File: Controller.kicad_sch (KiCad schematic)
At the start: 28 parts, among them IC3 STM32H563VGT6, U4 BMI088

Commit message: new update
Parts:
- removed C29, C30: 100nF, C0402C104K4RAC:CAPC1005X55N, symbol C0402C104K4RAC:C0402C104K4RAC
- removed U4: BMI088, Module:PQFN50P450X300X100-16N, symbol BMI088:BMI088
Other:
- moved on the sheet: R18

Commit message: new
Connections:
- net SCK: now reaches IC3.1 (PE2)
- net AR_A4: now reaches IC3.15 (PC0)
- net ETH_MDC: now reaches IC3.16 (PC1)
- net AR_A5: now reaches IC3.17 (PC2)
- net AR_MOSI: now reaches IC3.18 (PC3)
- net 50MHZOUT: now reaches IC3.24 (PA1)
- net ETH_MDIO: now reaches IC3.25 (PA2)
- net AR_SS: now reaches IC3.26 (PA3)
- net AR_A0: now reaches IC3.29 (PA4)
- net ETH_TX_EN: now reaches IC3.30 (PA5)
- net AR_A1: now reaches IC3.31 (PA6)
- net ETH_CRS_DV: now reaches IC3.32 (PA7)
- net ETH_RX_D0: now reaches IC3.33 (PC4)
- net ETH_RX_D1: now reaches IC3.34 (PC5)
- net AR_A2: now reaches IC3.35 (PB0)
- net AR_A3: now reaches IC3.36 (PB1)
- net SDI: now reaches IC3.4 (PE5)
- net ESP_BOOT: now reaches IC3.44 (PE13)
- net ESP_EN: now reaches IC3.45 (PE14)
- net SDO: now reaches IC3.5 (PE6)
- net ETH_TX_D0: now reaches IC3.51 (PB12)
- net AR_SCK: now reaches IC3.52 (PB13)
- net AR_MISO: now reaches IC3.53 (PB14)
- net ETH_TX_D1: now reaches IC3.54 (PB15)
- net AR_TX: now reaches IC3.55 (PD8)
- net AR_RX: now reaches IC3.56 (PD9)
- net AR_D4: now reaches IC3.57 (PD10)
- net AR_D5: now reaches IC3.58 (PD11)
- net AR_D6: now reaches IC3.59 (PD12)
- net AR_D7: now reaches IC3.60 (PD13)
- net AR_D8: now reaches IC3.61 (PD14)
- net AR_D9: now reaches IC3.62 (PD15)
- net AR_D2: now reaches IC3.63 (PC6)
- net AR_D3: now reaches IC3.64 (PC7)
- net ESP_TXD: now reaches IC3.68 (PA9)
- net ESP_RXD: now reaches IC3.69 (PA10)
- net GN_CS: now reaches IC3.77 (PA15)
- net GN_SDO: now reaches IC3.87 (PD6)
- net GN_SCK: now reaches IC3.89 (PB3)
- net GN_SDI: now reaches IC3.90 (PB4)
- net GN_TIMEPULSE: now reaches IC3.91 (PB5)
- net AR_SCL: now reaches IC3.92 (PB6)
- net AR_SDA: now reaches IC3.93 (PB7)
- net TX_READY: now reaches IC3.95 (PB8)
- net GN_EXINT: now reaches IC3.96 (PB9)

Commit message: new table
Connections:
- net CSB_ACCEL: now also IC3.42 (PE11)
- net CSB_GYRO: now also IC3.3 (PE4)
- net INT1_ACCEL: now also IC3.2 (PE3)
- net INT1_GYRO: now also IC3.8 (PC14-OSC32_IN)
- net INT2_ACCEL: now also IC3.7 (PC13)
- net INT2_GYRO: now also IC3.9 (PC15-OSC32_OUT)
- net RESET_GNSS: now also IC3.97 (PE0)
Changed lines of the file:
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@@
-		)
-	)
-	(text_box "CHECK THE PIN MAPPING FOR IMU"
-		(exclude_from_sim no)
-		(at 85.09 36.83 0)
-		(size 33.02 21.59)
-		(stroke
-			(width 0)
-			(type default)
-		)
-		(fill
-			(type color)
-			(color 114 255 146 1)
-		)
-		(effects
-			(font
-				(size 2.54 2.54)
-				(thickness 0.254)
-				(bold yes)
-			)
-			(justify left top)
-		)
-	)
-	(text_box "THE PIN MAPPING FOR GNSS RESET AND AR_A2 HAVE THE SAME PIN IN STM."
-		(exclude_from_sim no)
-		(at 33.02 33.02 0)
-		(size 35.56 26.67)
-		(stroke
-			(width 0)
-			(type default)
-		)
-		(fill
-			(type color)
-			(color 140 255 96 1)
-		)
-		(effects
-			(font
-				(size 2.54 2.54)
-			)
-			(justify left top)
 		)
 	)
@@
 	(global_label "INT2_ACCEL"
 		(shape input)
-		(at 106.68 52.07 0)
-		(fields_autoplaced yes)
-		(effects
-			(font
-				(size 1.27 1.27)
-			)
-			(justify left)
-		)
-		(property "Intersheetrefs" "${INTERSHEET_REFS}"
-			(at 120.5509 52.07 0)
-			(effects
-				(font
-					(size 1.27 1.27)
-				)
-				(justify left)
+		(at 143.51 86.36 180)
+		(fields_autoplaced yes)
+		(effects
+			(font
+				(size 1.27 1.27)
+			)
+			(justify right)
+		)
+		(property "Intersheetrefs" "${INTERSHEET_REFS}"
+			(at 129.6391 86.36 0)
+			(effects
+				(font
+					(size 1.27 1.27)
+				)
+				(justify right)
 				(hide yes)
 			)
@@
 	(global_label "INT1_ACCEL"
 		(shape input)
-		(at 106.68 49.53 0)
-		(fields_autoplaced yes)
-		(effects
-			(font
-				(size 1.27 1.27)
-			)
-			(justify left)
-		)
-		(property "Intersheetrefs" "${INTERSHEET_REFS}"
-			(at 120.5509 49.53 0)
-			(effects
-				(font
-					(size 1.27 1.27)
-				)
-				(justify left)
+		(at 143.51 73.66 180)
+		(fields_autoplaced yes)
+		(effects
+			(font
+				(size 1.27 1.27)
+			)
+			(justify right)
+		)
+		(property "Intersheetrefs" "${INTERSHEET_REFS}"
+			(at 129.6391 73.66 0)
+			(effects
+				(font
+					(size 1.27 1.27)
+				)
+				(justify right)
 				(hide yes)
 			)
@@
 	(global_label "INT1_GYRO"
 		(shape input)
-		(at 106.68 54.61 0)
-		(fields_autoplaced yes)
-		(effects
-			(font
-				(size 1.27 1.27)
-			)
-			(justify left)
-		)
-		(property "Intersheetrefs" "${INTERSHEET_REFS}"
-			(at 119.7043 54.61 0)
-			(effects
-				(font
-					(size 1.27 1.27)
-				)
-				(justify left)
+		(at 143.51 88.9 180)
+		(fields_autoplaced yes)
+		(effects
+			(font
+				(size 1.27 1.27)
+			)
+			(justify right)
+		)
+		(property "Intersheetrefs" "${INTERSHEET_REFS}"
+			(at 130.4857 88.9 0)
+			(effects
+				(font
+					(size 1.27 1.27)
+				)
+				(justify right)
 				(hide yes)
 			)
@@
 	(global_label "RESET_GNSS"
 		(shape input)
-		(at 72.39 58.42 180)
-		(fields_autoplaced yes)
-		(effects
-			(font
-				(size 1.27 1.27)
-			)
-			(justify right)
-		)
-		(property "Intersheetrefs" "${INTERSHEET_REFS}"
-			(at 57.6726 58.42 0)
-			(effects
-				(font
-					(size 1.27 1.27)
-				)
-				(justify right)
+		(at 158.75 53.34 90)
+		(fields_autoplaced yes)
+		(effects
+			(font
+				(size 1.27 1.27)
+			)
+			(justify left)
+		)
+		(property "Intersheetrefs" "${INTERSHEET_REFS}"
+			(at 158.75 38.6226 90)
+			(effects
+				(font
+					(size 1.27 1.27)
+				)
+				(justify left)
 				(hide yes)
 			)
@@
 	(global_label "CSB_ACCEL"
 		(shape input)
-		(at 95.25 55.88 180)
-		(fields_autoplaced yes)
-		(effects
-			(font
-				(size 1.27 1.27)
-			)
-			(justify right)
-		)
-		(property "Intersheetrefs" "${INTERSHEET_REFS}"
-			(at 81.742 55.88 0)
+		(at 191.77 149.86 270)
+		(fields_autoplaced yes)
+		(effects
+			(font
+				(size 1.27 1.27)
+			)
+			(justify right)
+		)
+		(property "Intersheetrefs" "${INTERSHEET_REFS}"
+			(at 191.77 163.368 90)
 			(effects
 				(font
@@
 	(global_label "INT2_GYRO"
 		(shape input)
-		(at 106.68 57.15 0)
-		(fields_autoplaced yes)
-		(effects
-			(font
-				(size 1.27 1.27)
-			)
-			(justify left)
-		)
-		(property "Intersheetrefs" "${INTERSHEET_REFS}"
-			(at 119.7043 57.15 0)
-			(effects
-				(font
-					(size 1.27 1.27)
-				)
-				(justify left)
+		(at 143.51 91.44 180)
+		(fields_autoplaced yes)
+		(effects
+			(font
+				(size 1.27 1.27)
+			)
+			(justify right)
+		)
+		(property "Intersheetrefs" "${INTERSHEET_REFS}"
+			(at 130.4857 91.44 0)
+			(effects
+				(font
+					(size 1.27 1.27)
+				)
+				(justify right)
 				(hide yes)
 			)
@@
 	(global_label "CSB_GYRO"
 		(shape input)
-		(at 93.98 52.07 180)
-		(fields_autoplaced yes)
-		(effects
-			(font
-				(size 1.27 1.27)
-			)
-			(justify right)
-		)
-		(property "Intersheetrefs" "${INTERSHEET_REFS}"
-			(at 81.3186 52.07 0)
-			(effects
-				(font
+		(at 143.51 76.2 180)
+		(fields_autoplaced yes)
+		(effects
+			(font
+				(size 1.27 1.27)
+			)
+			(justify right)
+		)
+		(property "Intersheetrefs" "${INTERSHEET_REFS}"
+			(at 130.8486 76.2 0)
+			(effects
+				(font

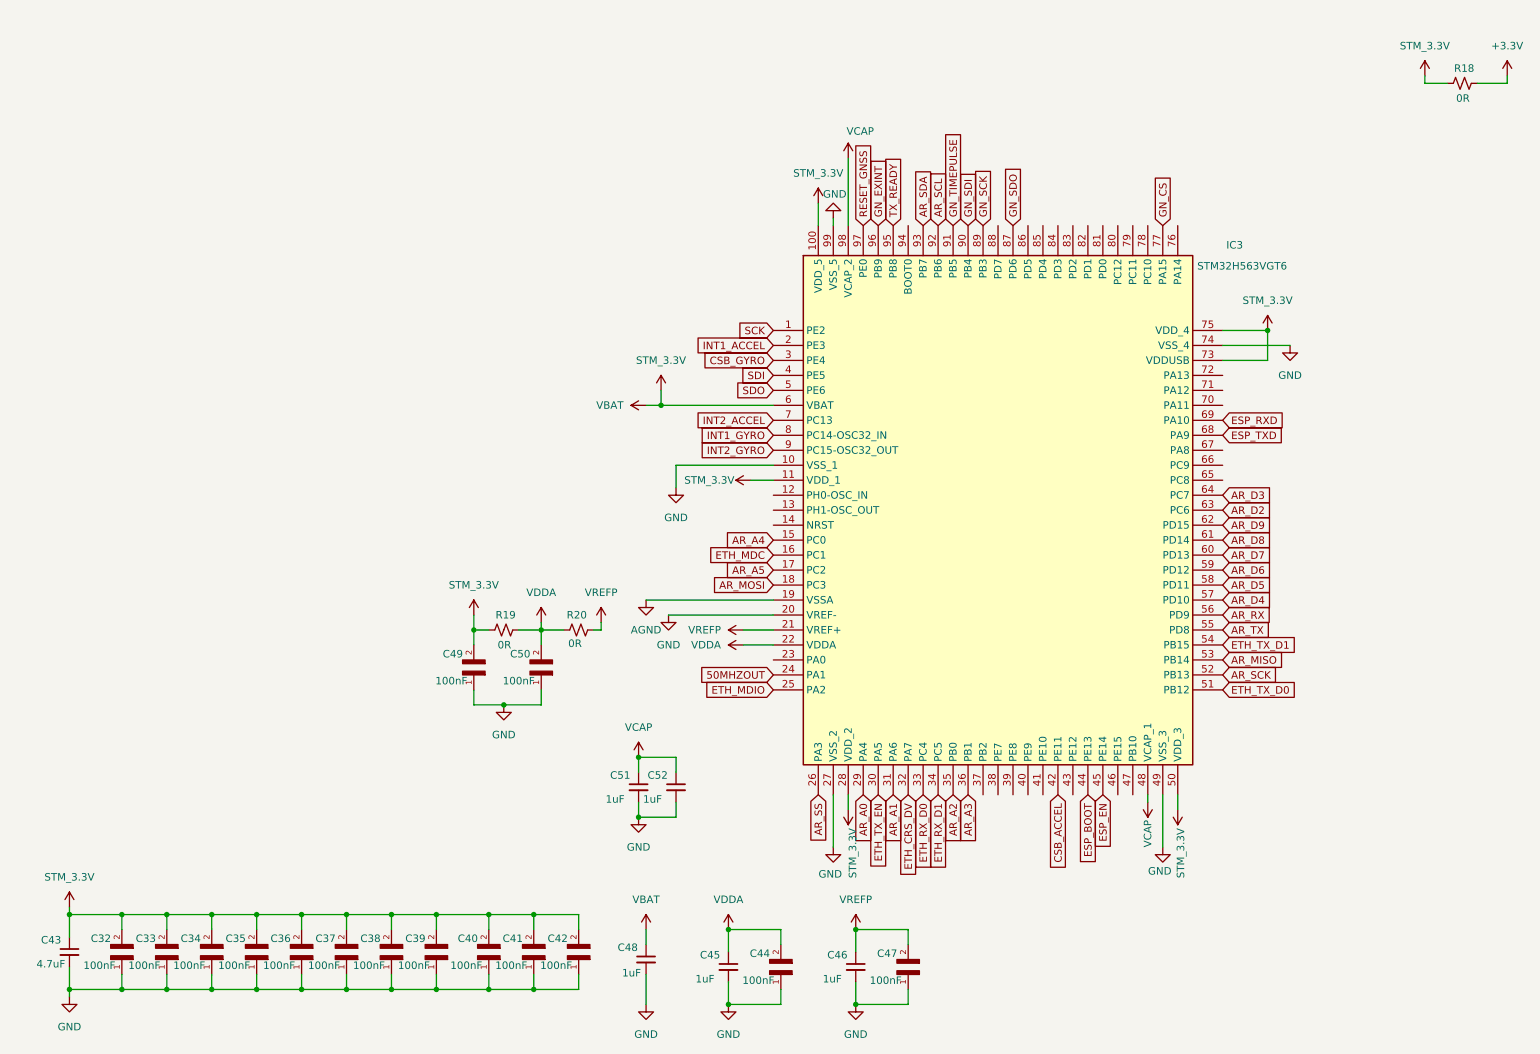
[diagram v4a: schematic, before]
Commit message: update the LED,SD card slot and new IMU
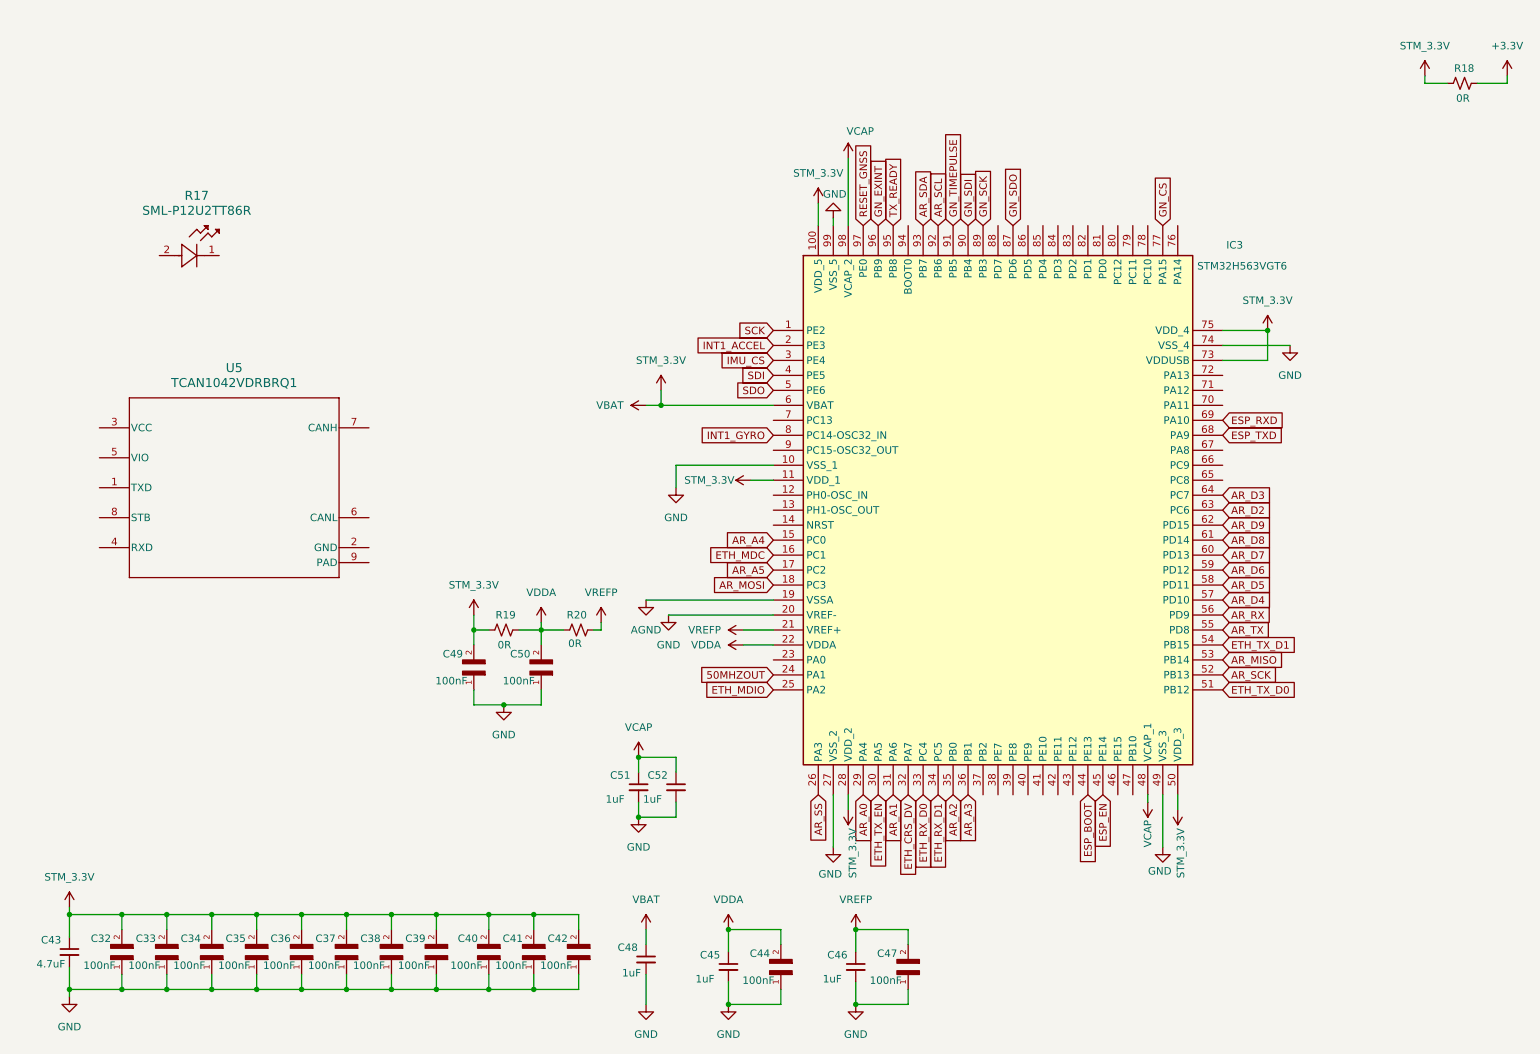
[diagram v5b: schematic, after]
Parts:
- added R17: SML-P12U2TT86R, GNSS_Library:LED_SML-P11D_ROM, symbol 2026-08-14_04-34-19:SML-P12U2TT86R
- added U5: TCAN1042VDRBRQ1, GNSS_Library:DRB0008F, symbol 2026-08-14_04-42-40:TCAN1042VDRBRQ1
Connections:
- net CSB_ACCEL: no longer names the net of IC3.42 (PE11)
- net CSB_GYRO renamed IMU_CS
- net INT2_ACCEL: no longer names the net of IC3.7 (PC13)
- net INT2_GYRO: no longer names the net of IC3.9 (PC15-OSC32_OUT)
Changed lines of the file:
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@@
 		)
 	)
-	(global_label "INT2_ACCEL"
-		(shape input)
-		(at 143.51 86.36 180)
-		(fields_autoplaced yes)
-		(effects
-			(font
-				(size 1.27 1.27)
-			)
-			(justify right)
-		)
-		(property "Intersheetrefs" "${INTERSHEET_REFS}"
-			(at 129.6391 86.36 0)
-			(effects
-				(font
-					(size 1.27 1.27)
-				)
-				(justify right)
-				(hide yes)
-			)
-		)
-	)
 	(global_label "AR_A5"
 		(shape input)
@@
 		)
 	)
-	(global_label "CSB_ACCEL"
-		(shape input)
-		(at 191.77 149.86 270)
-		(fields_autoplaced yes)
-		(effects
-			(font
-				(size 1.27 1.27)
-			)
-			(justify right)
-		)
-		(property "Intersheetrefs" "${INTERSHEET_REFS}"
-			(at 191.77 163.368 90)
-			(effects
-				(font
-					(size 1.27 1.27)
-				)
-				(justify right)
-				(hide yes)
-			)
-		)
-	)
-	(global_label "INT2_GYRO"
-		(shape input)
-		(at 143.51 91.44 180)
-		(fields_autoplaced yes)
-		(effects
-			(font
-				(size 1.27 1.27)
-			)
-			(justify right)
-		)
-		(property "Intersheetrefs" "${INTERSHEET_REFS}"
-			(at 130.4857 91.44 0)
-			(effects
-				(font
-					(size 1.27 1.27)
-				)
-				(justify right)
-				(hide yes)
-			)
-		)
-	)
 	(global_label "AR_MISO"
 		(shape input)
@@
 		)
 	)
-	(global_label "CSB_GYRO"
+	(global_label "IMU_CS"
 		(shape input)
 		(at 143.51 76.2 180)
@@
 		)
 		(property "Intersheetrefs" "${INTERSHEET_REFS}"
-			(at 130.8486 76.2 0)
+			(at 133.691 76.2 0)
 			(effects
 				(font
@@
 	)
 	(symbol
+		(lib_id "2026-08-14_04-42-40:TCAN1042VDRBRQ1")
+		(at 52.07 97.79 0)
+		(unit 1)
+		(exclude_from_sim no)
+		(in_bom yes)
+		(on_board yes)
+		(dnp no)
+		(fields_autoplaced yes)
+		(property "Reference" "U5"
+			(at 52.07 77.47 0)
+			(effects
+				(font
+					(size 1.524 1.524)
+				)
+			)
+		)
+		(property "Value" "TCAN1042VDRBRQ1"
+			(at 52.07 80.01 0)
+			(effects
+				(font
+					(size 1.524 1.524)
+				)
+			)
+		)
+		(property "Footprint" "GNSS_Library:DRB0008F"
+			(at 52.07 97.79 0)
+			(effects
+				(font
+					(size 1.27 1.27)
+					(italic yes)
+				)
+				(hide yes)
+			)
+		)
+		(property "Datasheet" "https://www.ti.com/lit/gpn/tcan1042v-q1"
+			(at 52.07 97.79 0)
+			(effects
+				(font
+					(size 1.27 1.27)
+					(italic yes)
+				)
+				(hide yes)
+			)
+		)
+		(property "Description" ""
+			(at 52.07 97.79 0)
+			(effects
+				(font
+					(size 1.27 1.27)
+				)
+				(hide yes)
+			)
+		)
+		(pin "7"
+		)
+		(pin "2"
+		)
+		(pin "5"
+		)
+		(pin "4"
+		)
+		(pin "8"
+		)
+		(pin "6"
+		)
+		(pin "9"
+		)
+		(pin "3"
+		)
+		(pin "1"
+		)
+		(instances
+			(project ""
+				(path "/a70dad34-b24c-4b58-b91c-f14576b5da7d/5f28e942-ada7-4d13-8727-49641d723651"
+					(reference "U5")
+					(unit 1)
+				)
+			)
+		)
+	)
+	(symbol
 		(lib_id "C0402C104K4RAC:C0402C104K4RAC")
 		(at 144.78 180.34 90)
@@
 					(unit 1)
 				)
+			)
+		)
+	)
+	(symbol
+		(lib_id "2026-08-14_04-34-19:SML-P12U2TT86R")
+		(at 39.37 58.42 0)
+		(unit 1)
+		(exclude_from_sim no)
+		(in_bom yes)
+		(on_board yes)
+		(dnp no)
+		(fields_autoplaced yes)
+		(property "Reference" "R17"
+			(at 45.72 48.26 0)
+			(effects
+				(font
+					(size 1.524 1.524)
+				)
+			)
+		)
+		(property "Value" "SML-P12U2TT86R"
+			(at 45.72 50.8 0)
+			(effects
+				(font
+					(size 1.524 1.524)
+				)
+			)
+		)
+		(property "Footprint" "GNSS_Library:LED_SML-P11D_ROM"
+			(at 39.37 58.42 0)
+			(effects
+				(font
+					(size 1.27 1.27)
+					(italic yes)
+				)
+				(hide yes)
+			)
+		)
+		(property "Datasheet" "SML-P12U2TT86R"
+			(at 39.37 58.42 0)
+			(effects
+				(font
+					(size 1.27 1.27)
+					(italic yes)
+				)
+				(hide yes)
+			)
+		)
+		(property "Description" ""
+			(at 39.37 58.42 0)
+			(effects
+				(font
+					(size 1.27 1.27)
+				)
+				(hide yes)
+			)
+		)
+		(pin "2"
+		)
+		(pin "1"
+		)
+		(instances
+			(project ""
+				(path "/a70dad34-b24c-4b58-b91c-f14576b5da7d/5f28e942-ada7-4d13-8727-49641d723651"
+					(reference "R17")
+					(unit 1)
+				)

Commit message: filter for CAN
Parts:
- added C68: 4.7nF, C0402C104K4RAC:CAPC1005X55N, symbol C0402C104K4RAC:C0402C104K4RAC
- added C69, C71: 100nF, C0402C104K4RAC:CAPC1005X55N, symbol C0402C104K4RAC:C0402C104K4RAC
- added C70, C72: 4.7uF, Capacitor_SMD:C_0805_2012Metric, symbol Device:C_Small
- added R25: SML-P12U2TT86R, GNSS_Library:LED_SML-P11D_ROM, symbol 2026-08-14_04-34-19:SML-P12U2TT86R
- added R26, R27: 60R, Resistor_SMD:R_0805_2012Metric, symbol Device:R_Small_US
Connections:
- net GND: now also U5.2 (GND), U5.9 (PAD), C68.1, C69.1, C70.2, C71.1, C72.2
- net VIN: now reaches U5.3 (VCC)
- net VIN: now also U5.5 (VIO), C69.2, C70.1, C71.2, C72.1
- net at U5.6 (CANL): now also R26.2
- net at U5.7 (CANH): now also R27.2
- new net: C68.2, R26.1, R27.1
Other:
- moved on the sheet: R17, U5

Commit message: new
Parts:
- added R28, R29: 560R, Resistor_SMD:R_0805_2012Metric, symbol Device:R_Small_US
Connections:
- net GND: now also R17.1, R25.1
- net CAN_TXD: now reaches U5.1 (TXD)
- net CAN_TXD: now also IC3.82 (PD1)
- net CAN_RXD: now reaches U5.4 (RXD)
- net CAN_RXD: now also IC3.81 (PD0)
- net CAN_STB: now reaches U5.8 (STB)
- net CAN_STB: now also IC3.88 (PD7)
- net at R25.2: now also R28.2
- net at R17.2: now also R29.2
- net GN_LED: now reaches IC3.84 (PD3)
- net GN_LED: now also R29.1
- net USER_LED: now reaches IC3.86 (PD5)
- net USER_LED: now also R28.1
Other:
- moved on the sheet: R17, R25

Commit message: new
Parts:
- added C73, C74: 100pF, C0402C104K4RAC:CAPC1005X55N, symbol C0402C104K4RAC:C0402C104K4RAC
- added D5, D6: ESD5V0D5-TP, ESD5V0D5TP, symbol ESD5V0D5-TP:ESD5V0D5-TP
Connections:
- net GND: now also C73.1, C74.1, D5.1 (K), D6.1 (K)
- net at R26.2, U5.6 (CANL): now also C74.2, D6.2 (A)
- net at R27.2, U5.7 (CANH): now also C73.2, D5.2 (A)
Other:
- moved on the sheet: C49, C50, C51, C52, C68, IC3, R19, R20, R26, R27, U5
